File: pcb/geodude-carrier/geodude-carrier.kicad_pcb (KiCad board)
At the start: 2 copper layers, 154.9 x 152.3 mm, 44 parts, among them J1 12V, J2 12V, J3 GND, J30 SCL, J31 SCL, J32 SDA, J33 SDA, J34 3V3, J35 3V3, J36 5V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

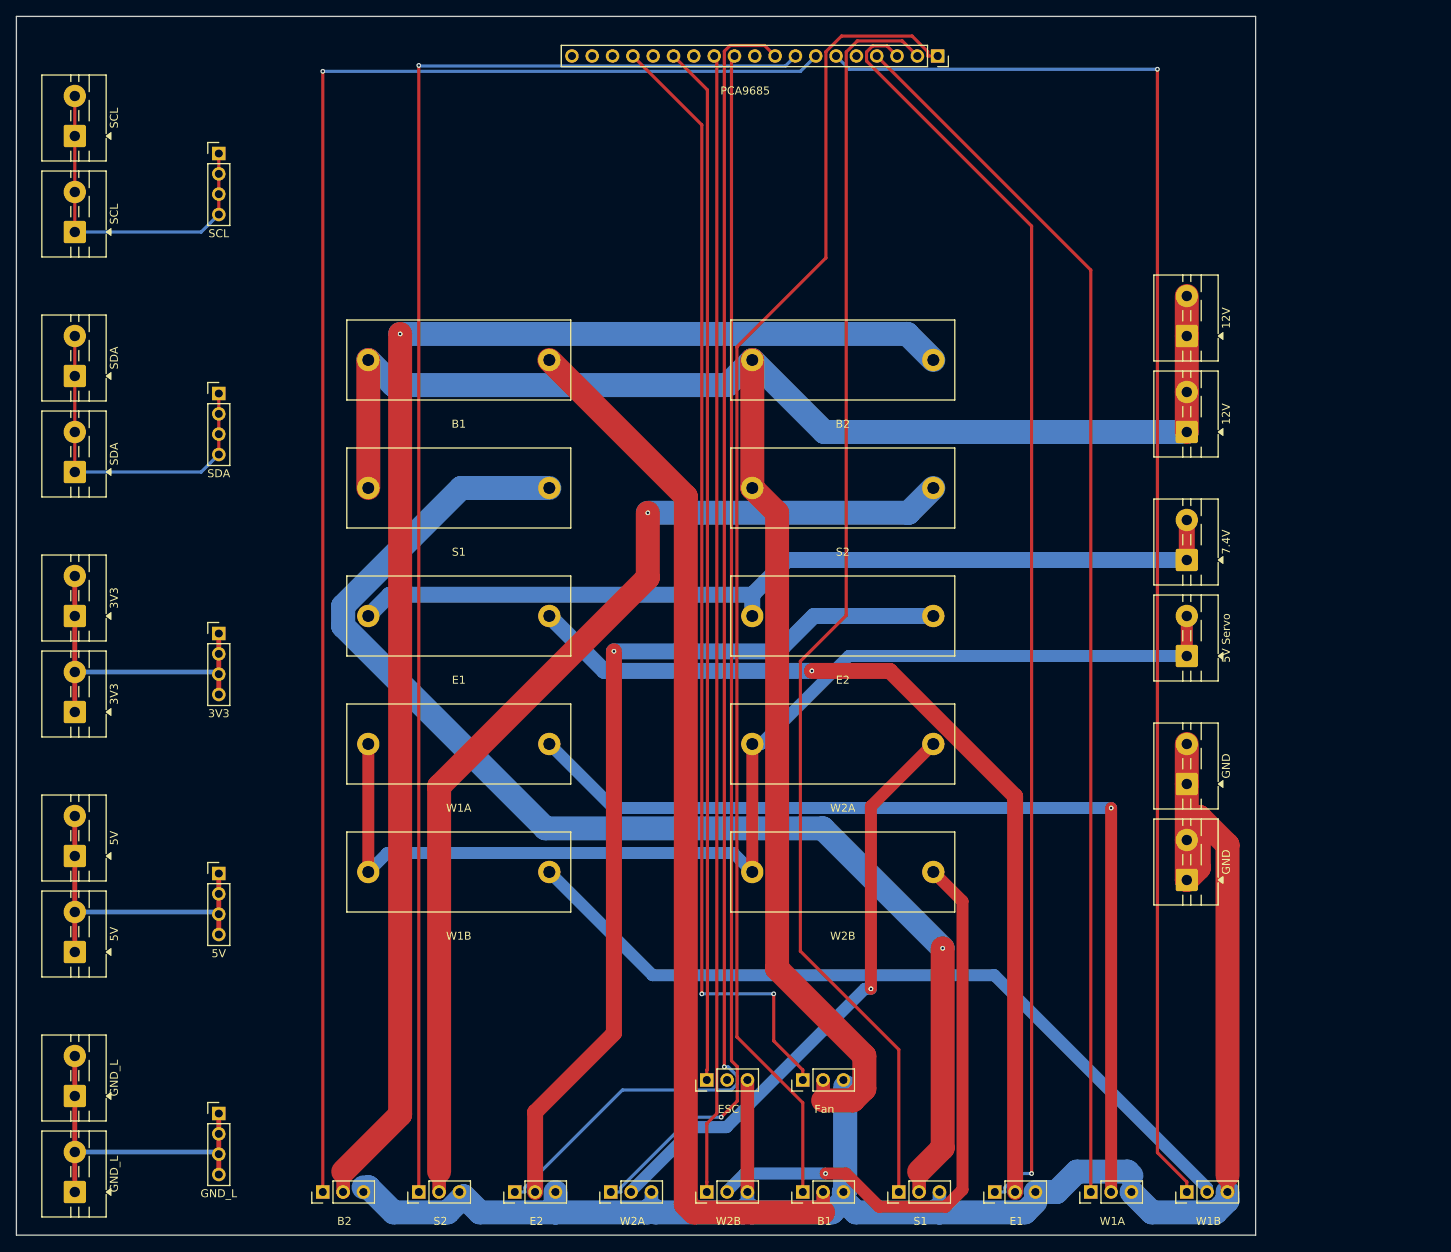
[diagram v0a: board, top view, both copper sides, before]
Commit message: Re-routed with default clearance, 2 unconnected remaining, via sizing needs work
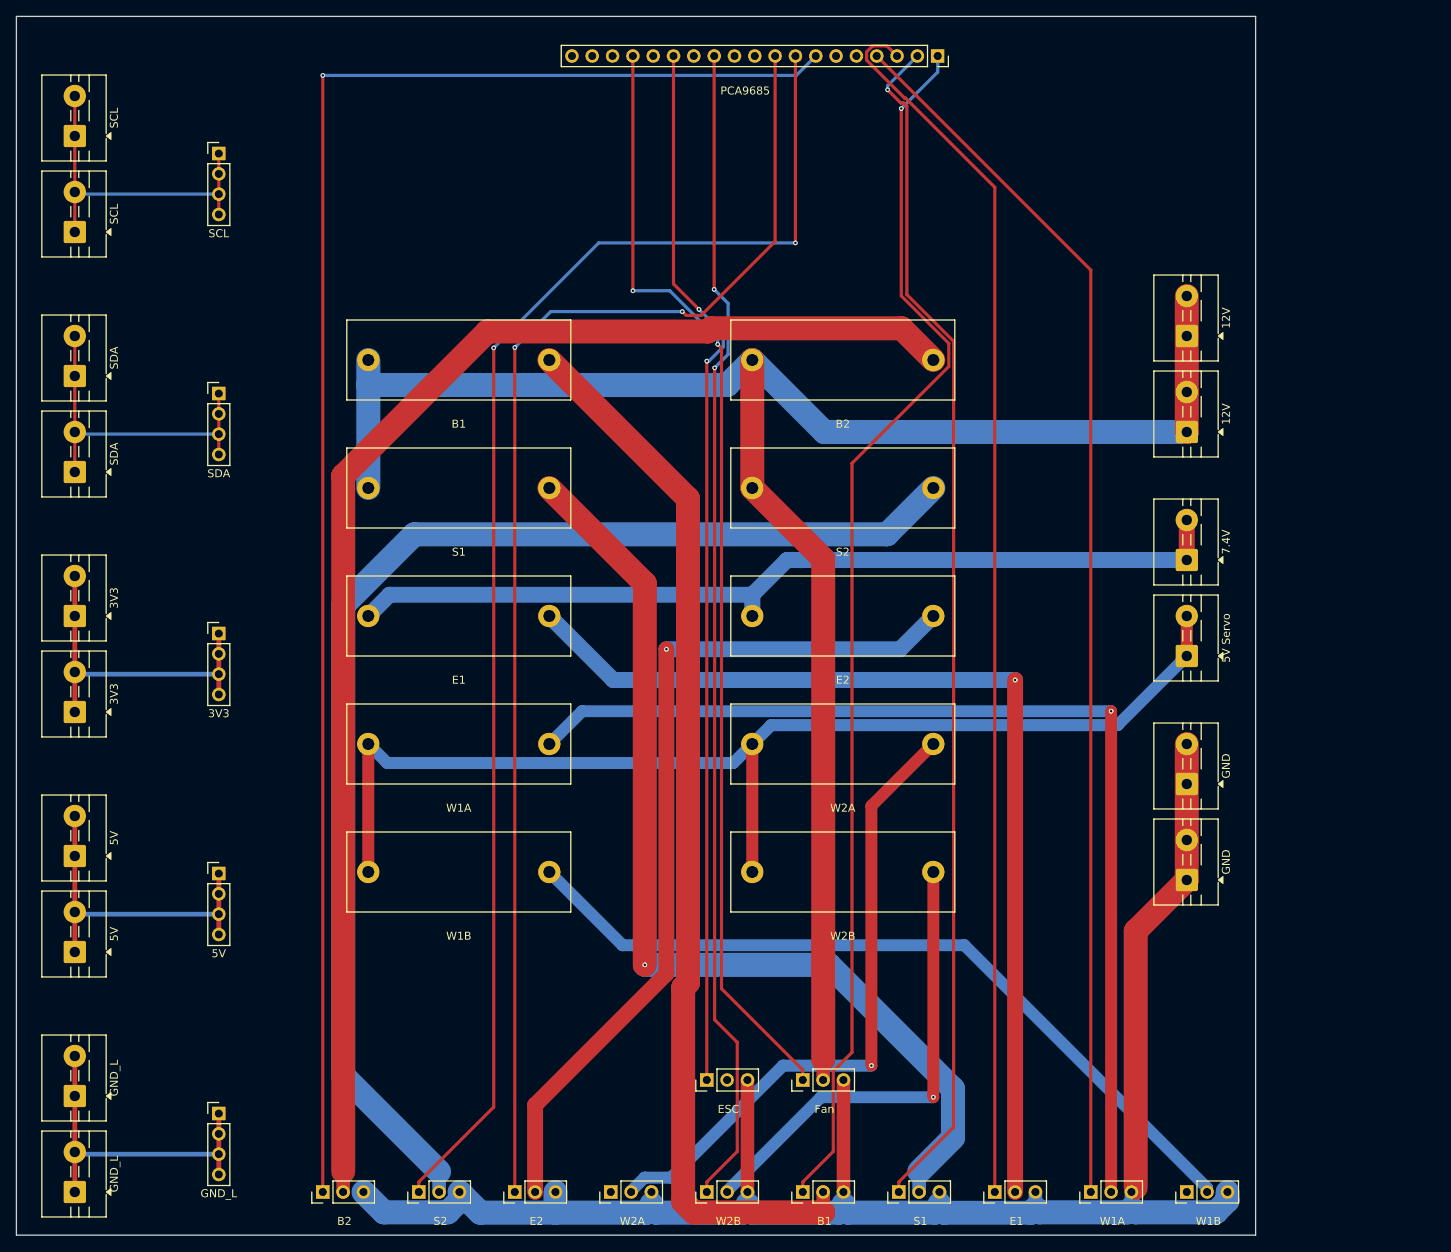
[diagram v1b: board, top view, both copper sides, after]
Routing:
- net PWM_CH4: track 182.7 -> 0.00 mm, vias 1 -> 0
- net PWM_CH8: track 151.9 -> 0.00 mm, vias 1 -> 0
- net SV2_PWR: track 157.7 -> 124.1 mm
- net SV7_PWR: track 132.7 -> 158.1 mm, vias 1 -> 0
- net GND: track 234.7 -> 217.6 mm
- net SV10_PWR: track 74.3 -> 58.9 mm
- net +12V: track 246.9 -> 234.0 mm
- net PWM_CH0: track 166.7 -> 153.9 mm, vias 0 -> 1
- net PWM_CH6: track 188.4 -> 175.9 mm, vias 1 -> 2
- net SV4_PWR: track 121.5 -> 132.0 mm
- net PWM_CH1: track 160.2 -> 150.0 mm, vias 0 -> 1
- net SV3_PWR: track 117.0 -> 125.5 mm
- net SV9_PWR: track 74.4 -> 80.1 mm
- net SV6_PWR: track 178.2 -> 172.6 mm, vias 1 -> 0
- net PWM_CH2: track 159.3 -> 153.9 mm, vias 1 -> 0
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
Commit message: Bigger vias, parallel power vias added, JLCPCB free tier via size
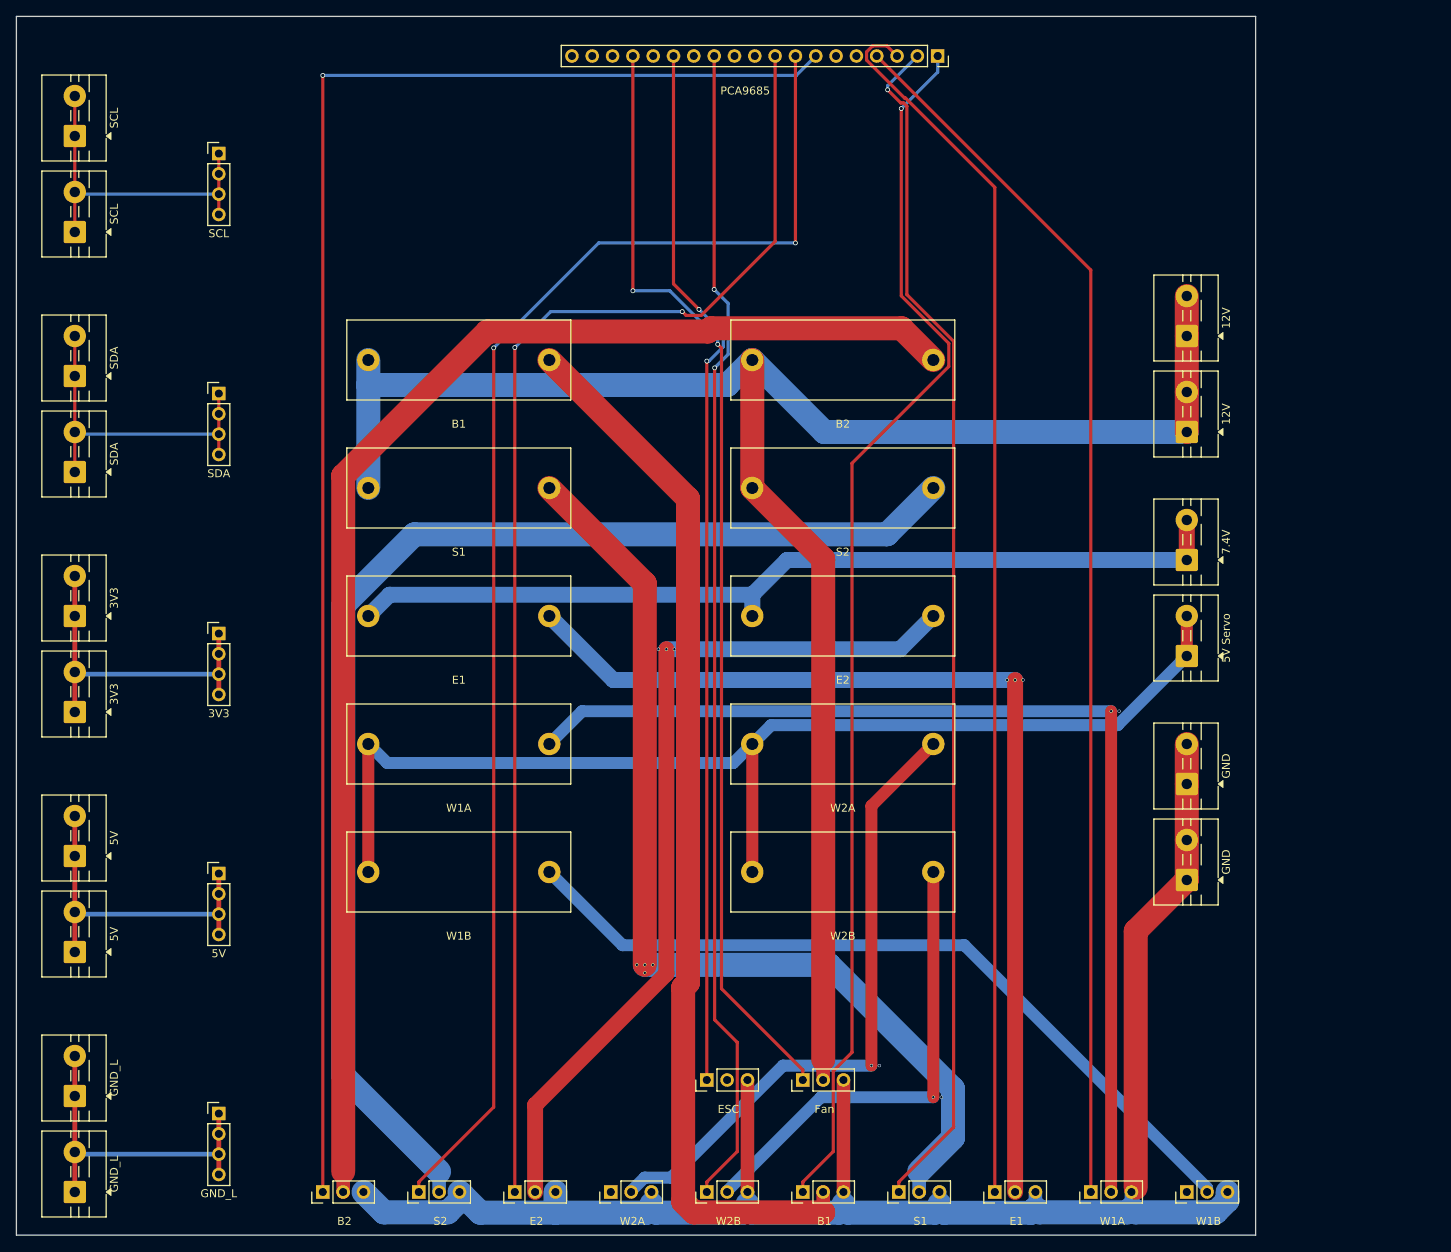
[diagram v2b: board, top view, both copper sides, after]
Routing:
- net SV9_PWR: vias 1 -> 2
- net SV8_PWR: vias 1 -> 3
- net SV4_PWR: vias 1 -> 2
- net SV3_PWR: vias 1 -> 3
- net SV2_PWR: vias 1 -> 5

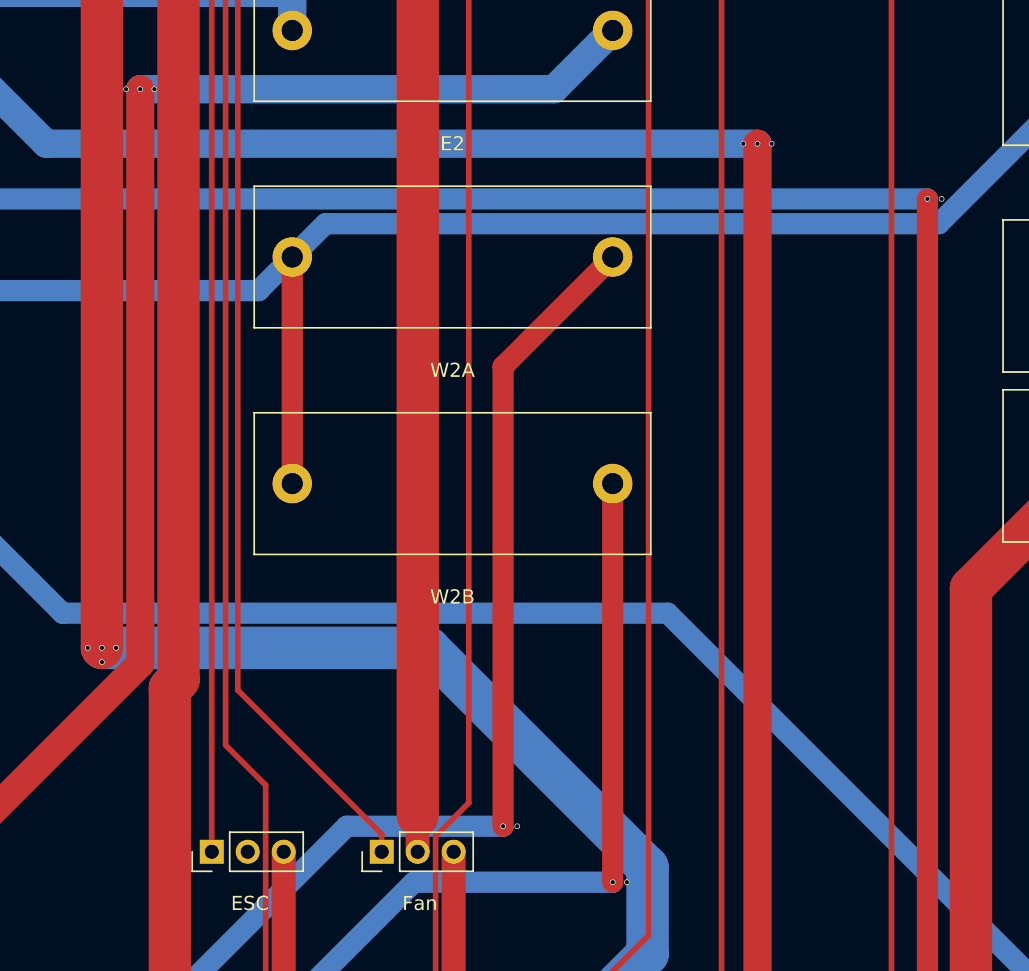
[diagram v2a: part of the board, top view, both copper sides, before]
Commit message: Clean route with 0.8mm power vias, 2 unconnected remaining
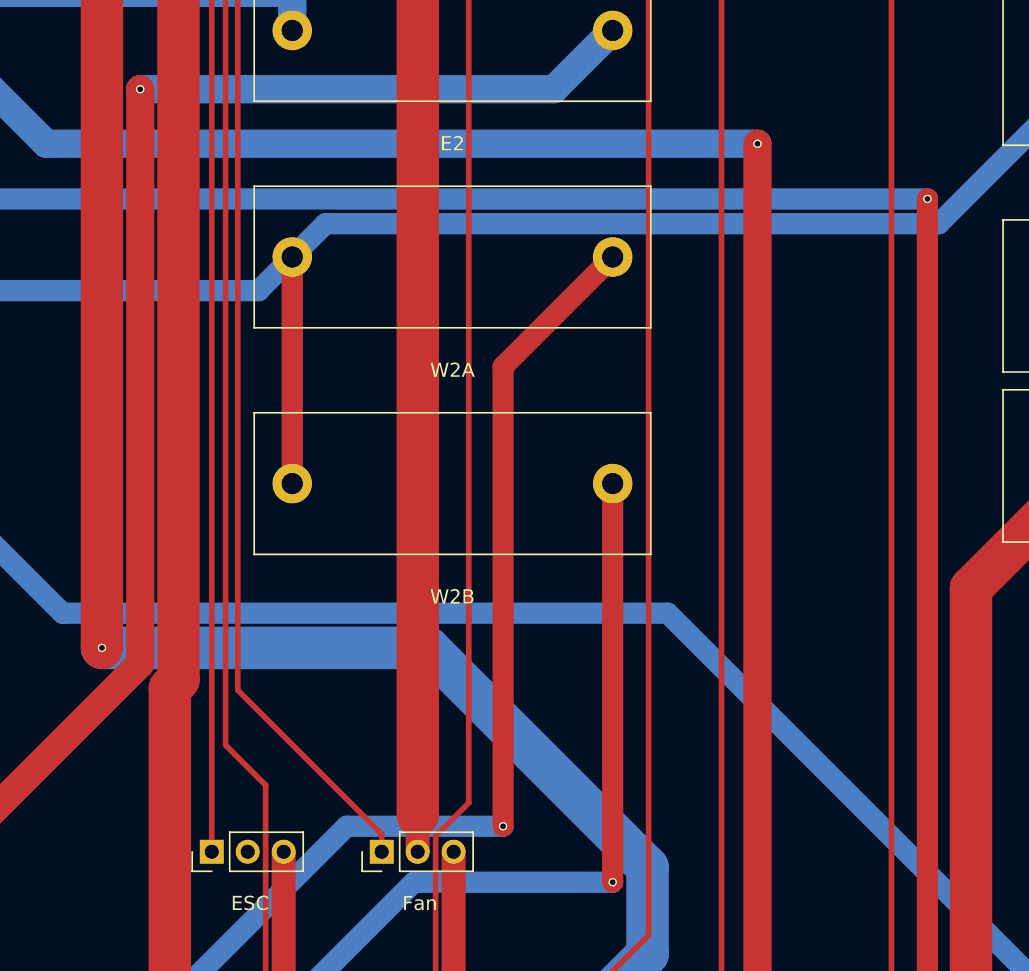
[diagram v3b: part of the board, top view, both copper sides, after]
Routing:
- net SV9_PWR: vias 2 -> 1
- net SV8_PWR: vias 3 -> 1
- net SV4_PWR: vias 2 -> 1
- net SV3_PWR: vias 3 -> 1
- net SV2_PWR: vias 5 -> 1
